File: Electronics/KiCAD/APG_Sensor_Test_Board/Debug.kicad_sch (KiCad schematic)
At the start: 0 parts

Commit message: debug schematic done
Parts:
- added BZ?: Buzzer, symbol Device:Buzzer
- added D? (x3): LED, symbol Device:LED
- added R? (x3): 200, symbol Device:R
- added R?: 10k, symbol Device:R
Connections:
- new net: BZ?.1 (+), R?.2
- new net: D?.2 (A), R?.2 (x3)
- new net Buzzer: R?.1
- new net Debug 1: R?.1
- new net Debug 2: R?.1
- new net Debug 3: R?.1
- new net GND: BZ?.2 (-), D?.1 (K), D?.1 (K), D?.1 (K)

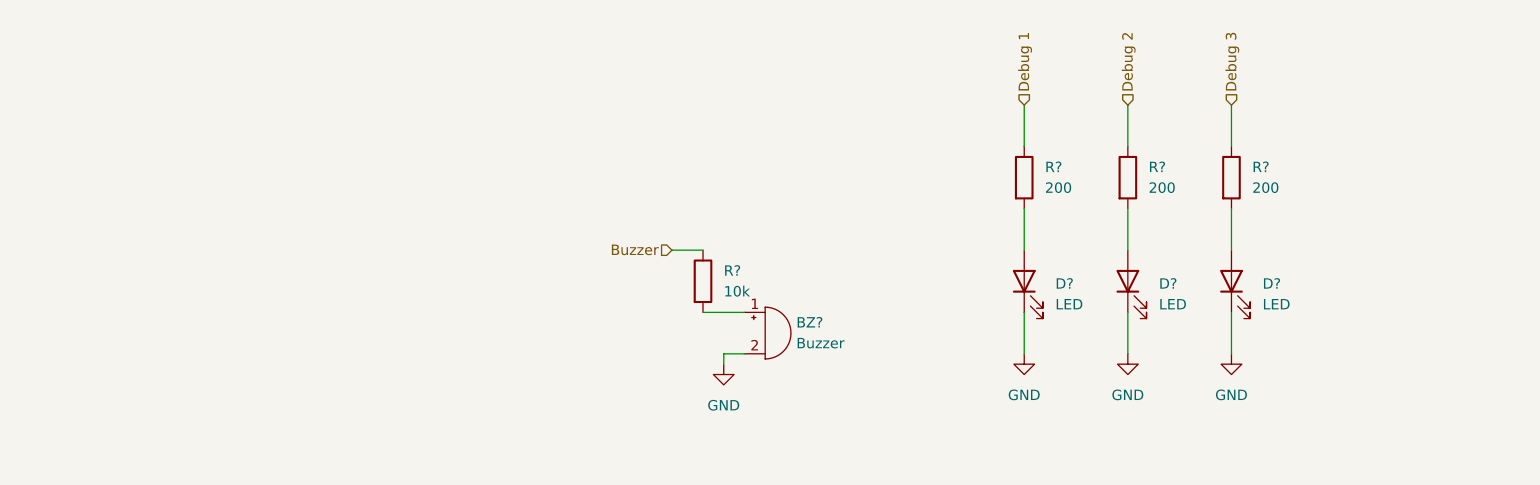
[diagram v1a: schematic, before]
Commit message: Gannon inspection decision to change IMU
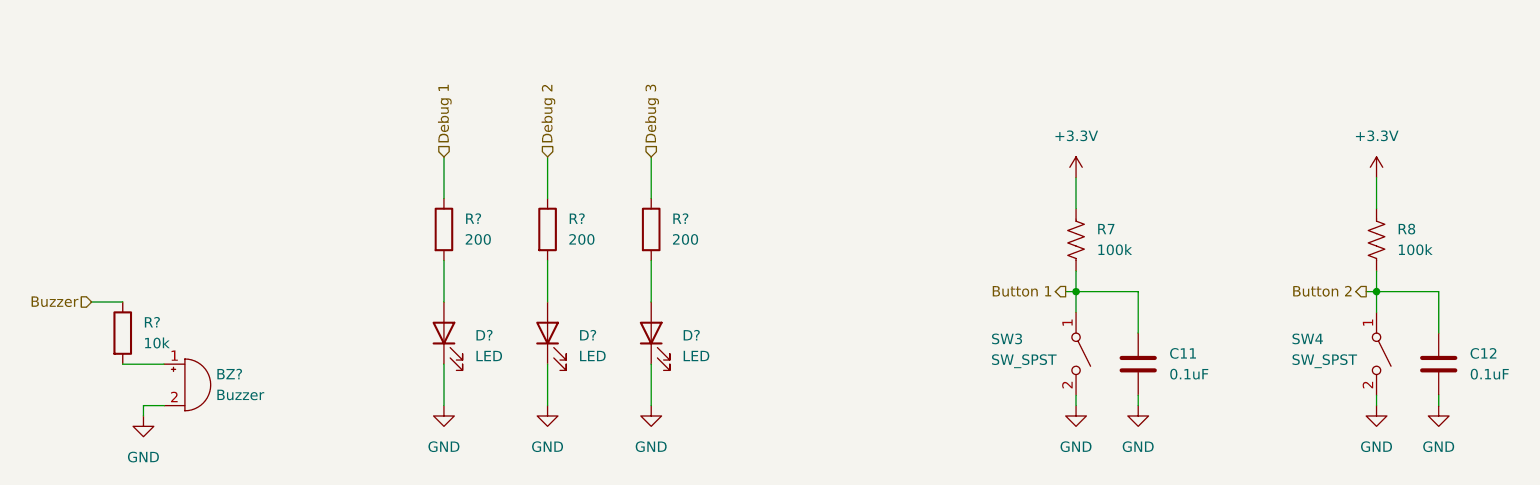
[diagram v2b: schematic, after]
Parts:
- added C11, C12: 0.1uF, symbol Device:C
- added R7, R8: 100k, symbol Device:R_US
- added SW3, SW4: SW_SPST, Button_Switch_SMD:SW_MEC_5GSH9, symbol Switch:SW_SPST
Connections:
- net GND: now also C11.2, C12.2, SW3.2 (B), SW4.2 (B)
- new net +3.3V: R7.1, R8.1
- new net Button 1: C11.1, R7.2, SW3.1 (A)
- new net Button 2: C12.1, R8.2, SW4.1 (A)
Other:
- moved on the sheet: BZ?, D?, R?

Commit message: reaninotate and begin footprints
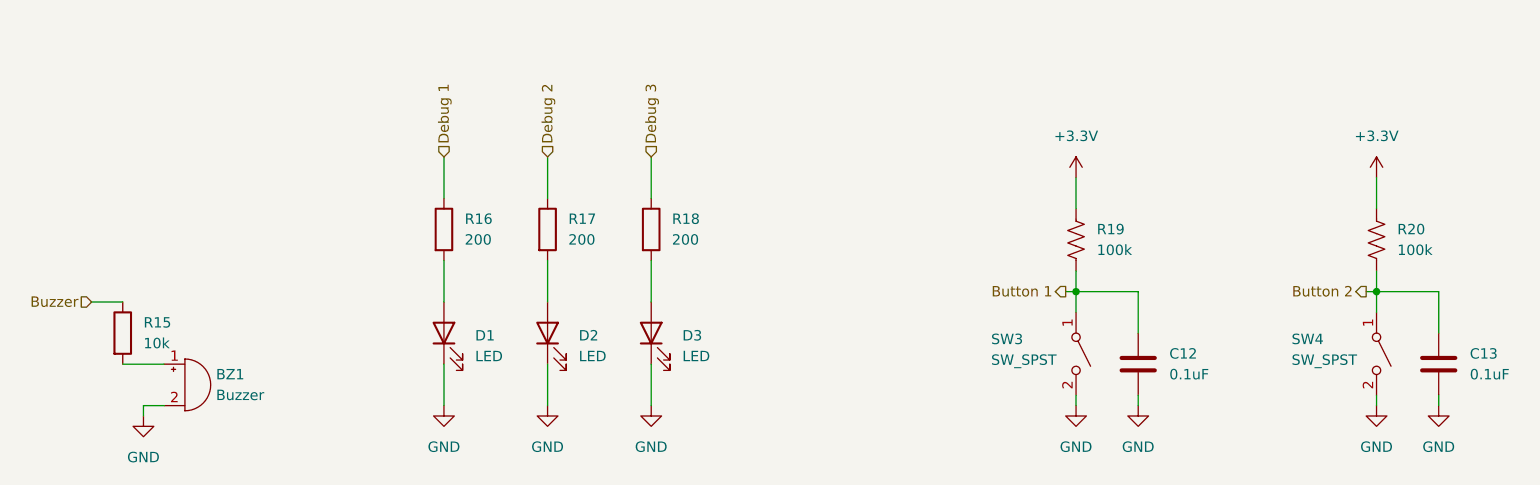
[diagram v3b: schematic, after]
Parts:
- C12: renamed from C11; footprint (none) -> Capacitor_SMD:C_0805_2012Metric
- C13: renamed from C12; footprint (none) -> Capacitor_SMD:C_0805_2012Metric
- R15, R16, R17, R18: renamed from R?; footprint (none) -> Resistor_SMD:R_0805_2012Metric
- R19: renamed from R7; footprint (none) -> Resistor_SMD:R_0805_2012Metric
- R20: renamed from R8; footprint (none) -> Resistor_SMD:R_0805_2012Metric
- gave numbers to parts that had none: 4
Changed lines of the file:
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@@
 		(dnp no)
 		(fields_autoplaced yes)
-		(property "Reference" "#PWR?"
+		(property "Reference" "#PWR036"
 			(at 106.68 101.6 0)
 			(effects
@@
 			(project "APG_Sensor_Test_Board"
 				(path "/3161be0c-372f-463d-be0a-bab00f344057/a925c584-3e41-45ac-af60-4ecbe46e87fc"
-					(reference "#PWR?")
+					(reference "#PWR036")
 					(unit 1)
 				)
@@
 		(dnp no)
 		(fields_autoplaced yes)
-		(property "Reference" "BZ?"
+		(property "Reference" "BZ1"
 			(at 78.74 91.4399 0)
 			(effects
@@
 			(project "APG_Sensor_Test_Board"
 				(path "/3161be0c-372f-463d-be0a-bab00f344057/a925c584-3e41-45ac-af60-4ecbe46e87fc"
-					(reference "BZ?")
+					(reference "BZ1")
 					(unit 1)
 				)
@@
 		(on_board yes)
 		(dnp no)
-		(property "Reference" "R7"
+		(property "Reference" "R19"
 			(at 186.69 73.6599 0)
 			(effects
@@
 			)
 		)
-		(property "Footprint" ""
+		(property "Footprint" "Resistor_SMD:R_0805_2012Metric"
 			(at 185.166 75.184 90)
 			(effects
@@
 			(project "APG_Sensor_Test_Board"
 				(path "/3161be0c-372f-463d-be0a-bab00f344057/a925c584-3e41-45ac-af60-4ecbe46e87fc"
-					(reference "R7")
+					(reference "R19")
 					(unit 1)
 				)
@@
 		(dnp no)
 		(fields_autoplaced yes)
-		(property "Reference" "#PWR031"
+		(property "Reference" "#PWR042"
 			(at 220.98 71.12 0)
 			(effects
@@
 			(project "APG_Sensor_Test_Board"
 				(path "/3161be0c-372f-463d-be0a-bab00f344057/a925c584-3e41-45ac-af60-4ecbe46e87fc"
-					(reference "#PWR031")
+					(reference "#PWR042")
 					(unit 1)
 				)
@@
 		(dnp no)
 		(fields_autoplaced yes)
-		(property "Reference" "#PWR032"
+		(property "Reference" "#PWR043"
 			(at 220.98 101.6 0)
 			(effects
@@
 			(project "APG_Sensor_Test_Board"
 				(path "/3161be0c-372f-463d-be0a-bab00f344057/a925c584-3e41-45ac-af60-4ecbe46e87fc"
-					(reference "#PWR032")
+					(reference "#PWR043")
 					(unit 1)
 				)
@@
 		(dnp no)
 		(fields_autoplaced yes)
-		(property "Reference" "#PWR029"
+		(property "Reference" "#PWR040"
 			(at 184.15 101.6 0)
 			(effects
@@
 			(project "APG_Sensor_Test_Board"
 				(path "/3161be0c-372f-463d-be0a-bab00f344057/a925c584-3e41-45ac-af60-4ecbe46e87fc"
-					(reference "#PWR029")
+					(reference "#PWR040")
 					(unit 1)
 				)
@@
 		(on_board yes)
 		(dnp no)
-		(property "Reference" "R8"
+		(property "Reference" "R20"
 			(at 223.52 73.6599 0)
 			(effects
@@
 			)
 		)
-		(property "Footprint" ""
+		(property "Footprint" "Resistor_SMD:R_0805_2012Metric"
 			(at 221.996 75.184 90)
 			(effects
@@
 			(project "APG_Sensor_Test_Board"
 				(path "/3161be0c-372f-463d-be0a-bab00f344057/a925c584-3e41-45ac-af60-4ecbe46e87fc"
-					(reference "R8")
+					(reference "R20")
 					(unit 1)
 				)
@@
 		(dnp no)
 		(fields_autoplaced yes)
-		(property "Reference" "R?"
+		(property "Reference" "R18"
 			(at 134.62 72.3899 0)
 			(effects
@@
 			)
 		)
-		(property "Footprint" ""
+		(property "Footprint" "Resistor_SMD:R_0805_2012Metric"
 			(at 130.302 73.66 90)
 			(effects
@@
 			(project "APG_Sensor_Test_Board"
 				(path "/3161be0c-372f-463d-be0a-bab00f344057/a925c584-3e41-45ac-af60-4ecbe46e87fc"
-					(reference "R?")
+					(reference "R18")
 					(unit 1)
 				)
@@
 		(dnp no)
 		(fields_autoplaced yes)
-		(property "Reference" "R?"
+		(property "Reference" "R15"
 			(at 69.85 85.0899 0)
 			(effects
@@
 			)
 		)
-		(property "Footprint" ""
+		(property "Footprint" "Resistor_SMD:R_0805_2012Metric"
 			(at 65.532 86.36 90)
 			(effects
@@
 			(project "APG_Sensor_Test_Board"
 				(path "/3161be0c-372f-463d-be0a-bab00f344057/a925c584-3e41-45ac-af60-4ecbe46e87fc"
-					(reference "R?")
+					(reference "R15")
 					(unit 1)
 				)
@@
 		(dnp no)
 		(fields_autoplaced yes)
-		(property "Reference" "#PWR?"
+		(property "Reference" "#PWR035"
 			(at 69.85 102.87 0)
 			(effects
@@
 			(project "APG_Sensor_Test_Board"
 				(path "/3161be0c-372f-463d-be0a-bab00f344057/a925c584-3e41-45ac-af60-4ecbe46e87fc"
-					(reference "#PWR?")
+					(reference "#PWR035")
 					(unit 1)
 				)
@@
 		(dnp no)
 		(fields_autoplaced yes)
-		(property "Reference" "#PWR?"
+		(property "Reference" "#PWR038"
 			(at 132.08 101.6 0)
 			(effects
@@
 			(project "APG_Sensor_Test_Board"
 				(path "/3161be0c-372f-463d-be0a-bab00f344057/a925c584-3e41-45ac-af60-4ecbe46e87fc"
-					(reference "#PWR?")
+					(reference "#PWR038")
 					(unit 1)
 				)
@@
 		(dnp no)
 		(fields_autoplaced yes)
-		(property "Reference" "#PWR?"
+		(property "Reference" "#PWR037"
 			(at 119.38 101.6 0)
 			(effects
@@
 			(project "APG_Sensor_Test_Board"
 				(path "/3161be0c-372f-463d-be0a-bab00f344057/a925c584-3e41-45ac-af60-4ecbe46e87fc"
-					(reference "#PWR?")
+					(reference "#PWR037")
 					(unit 1)
 				)
@@
 		(dnp no)
 		(fields_autoplaced yes)
-		(property "Reference" "R?"
+		(property "Reference" "R17"
 			(at 121.92 72.3899 0)
 			(effects
@@
 			)
 		)
-		(property "Footprint" ""
+		(property "Footprint" "Resistor_SMD:R_0805_2012Metric"
 			(at 117.602 73.66 90)
 			(effects
@@
 			(project "APG_Sensor_Test_Board"
 				(path "/3161be0c-372f-463d-be0a-bab00f344057/a925c584-3e41-45ac-af60-4ecbe46e87fc"
-					(reference "R?")
+					(reference "R17")
 					(unit 1)
 				)
@@
 		(dnp no)
 		(fields_autoplaced yes)
-		(property "Reference" "D?"
+		(property "Reference" "D2"
 			(at 123.19 86.6774 90)
 			(effects
@@
 			(project "APG_Sensor_Test_Board"
 				(path "/3161be0c-372f-463d-be0a-bab00f344057/a925c584-3e41-45ac-af60-4ecbe46e87fc"
-					(reference "D?")
+					(reference "D2")
 					(unit 1)
 				)
@@
 		(dnp no)
 		(fields_autoplaced yes)
-		(property "Reference" "D?"
+		(property "Reference" "D1"
 			(at 110.49 86.6774 90)
 			(effects
@@
 			(project "APG_Sensor_Test_Board"
 				(path "/3161be0c-372f-463d-be0a-bab00f344057/a925c584-3e41-45ac-af60-4ecbe46e87fc"
-					(reference "D?")
+					(reference "D1")
 					(unit 1)
 				)
@@
 		(dnp no)
 		(fields_autoplaced yes)
-		(property "Reference" "#PWR033"
+		(property "Reference" "#PWR044"
 			(at 228.6 101.6 0)
 			(effects
@@
 			(project "APG_Sensor_Test_Board"
 				(path "/3161be0c-372f-463d-be0a-bab00f344057/a925c584-3e41-45ac-af60-4ecbe46e87fc"
-					(reference "#PWR033")
+					(reference "#PWR044")
 					(unit 1)
 				)
@@
 		(dnp no)
 		(fields_autoplaced yes)
-		(property "Reference" "C12"
+		(property "Reference" "C13"
 			(at 232.41 88.8999 0)
 			(effects
@@
 			)
 		)
-		(property "Footprint" ""
+		(property "Footprint" "Capacitor_SMD:C_0805_2012Metric"
 			(at 229.5652 93.98 0)
 			(effects
@@
 			(project "APG_Sensor_Test_Board"
 				(path "/3161be0c-372f-463d-be0a-bab00f344057/a925c584-3e41-45ac-af60-4ecbe46e87fc"
-					(reference "C12")
+					(reference "C13")
 					(unit 1)
 				)
@@
 		(dnp no)
 		(fields_autoplaced yes)
-		(property "Reference" "C11"
+		(property "Reference" "C12"
 			(at 195.58 88.8999 0)
 			(effects
@@
 			)
 		)
-		(property "Footprint" ""
+		(property "Footprint" "Capacitor_SMD:C_0805_2012Metric"
 			(at 192.7352 93.98 0)
 			(effects
@@
 			(project "APG_Sensor_Test_Board"
 				(path "/3161be0c-372f-463d-be0a-bab00f344057/a925c584-3e41-45ac-af60-4ecbe46e87fc"
-					(reference "C11")
+					(reference "C12")
 					(unit 1)
 				)
@@
 		(dnp no)
 		(fields_autoplaced yes)
-		(property "Reference" "D?"
+		(property "Reference" "D3"
 			(at 135.89 86.6774 90)
 			(effects
@@
 			(project "APG_Sensor_Test_Board"
 				(path "/3161be0c-372f-463d-be0a-bab00f344057/a925c584-3e41-45ac-af60-4ecbe46e87fc"
-					(reference "D?")
+					(reference "D3")
 					(unit 1)
 				)
@@
 		(dnp no)
 		(fields_autoplaced yes)
-		(property "Reference" "R?"
+		(property "Reference" "R16"
 			(at 109.22 72.3899 0)
 			(effects
@@
 			)
 		)
-		(property "Footprint" ""
+		(property "Footprint" "Resistor_SMD:R_0805_2012Metric"
 			(at 104.902 73.66 90)
 			(effects
@@
 			(project "APG_Sensor_Test_Board"
 				(path "/3161be0c-372f-463d-be0a-bab00f344057/a925c584-3e41-45ac-af60-4ecbe46e87fc"
-					(reference "R?")
+					(reference "R16")
 					(unit 1)
 				)
@@
 		(dnp no)
 		(fields_autoplaced yes)
-		(property "Reference" "#PWR030"
+		(property "Reference" "#PWR041"
 			(at 191.77 101.6 0)
 			(effects
@@
 			(project "APG_Sensor_Test_Board"
 				(path "/3161be0c-372f-463d-be0a-bab00f344057/a925c584-3e41-45ac-af60-4ecbe46e87fc"
-					(reference "#PWR030")
+					(reference "#PWR041")
 					(unit 1)
 				)
@@
 		(dnp no)
 		(fields_autoplaced yes)
-		(property "Reference" "#PWR028"
+		(property "Reference" "#PWR039"
 			(at 184.15 71.12 0)
 			(effects
@@
 			(project "APG_Sensor_Test_Board"
 				(path "/3161be0c-372f-463d-be0a-bab00f344057/a925c584-3e41-45ac-af60-4ecbe46e87fc"
-					(reference "#PWR028")
-					(unit 1)
-				)
+					(reference "#PWR039")
+					(unit 1)
+				)

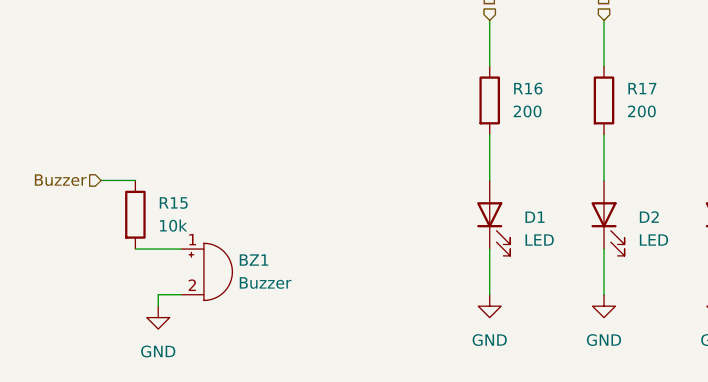
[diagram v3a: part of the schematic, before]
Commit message: completed footprint assignment
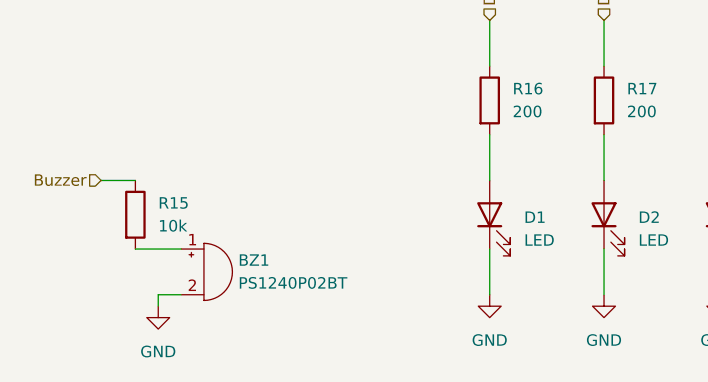
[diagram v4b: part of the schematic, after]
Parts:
- BZ1: value Buzzer -> PS1240P02BT; footprint (none) -> Buzzer_Beeper:Buzzer_TDK_PS1240P02BT_D12.2mm_H6.5mm
- D1, D2, D3: footprint (none) -> LED_SMD:LED_0805_2012Metric
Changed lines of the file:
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@@
 			)
 		)
-		(property "Value" "Buzzer"
+		(property "Value" "PS1240P02BT"
 			(at 78.74 93.9799 0)
 			(effects
@@
 			)
 		)
-		(property "Footprint" ""
+		(property "Footprint" "Buzzer_Beeper:Buzzer_TDK_PS1240P02BT_D12.2mm_H6.5mm"
 			(at 74.295 90.17 90)
 			(effects
@@
 		)
 		(property "Description" "Buzzer, polarized"
+			(at 74.93 92.71 0)
+			(effects
+				(font
+					(size 1.27 1.27)
+				)
+				(hide yes)
+			)
+		)
+		(property "JLCPCB" ""
 			(at 74.93 92.71 0)
 			(effects
@@
 			)
 		)
-		(property "Footprint" ""
+		(property "Footprint" "LED_SMD:LED_0805_2012Metric"
 			(at 119.38 86.36 0)
 			(effects
@@
 			)
 		)
-		(property "Footprint" ""
+		(property "Footprint" "LED_SMD:LED_0805_2012Metric"
 			(at 106.68 86.36 0)
 			(effects
@@
 			)
 		)
-		(property "Footprint" ""
+		(property "Footprint" "LED_SMD:LED_0805_2012Metric"
 			(at 132.08 86.36 0)
 			(effects

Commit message: JLC part numbers
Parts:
- D1: value LED -> Yellow; JLCPCB (none) -> C2296
- D2: value LED -> Green; JLCPCB (none) -> C2297
- D3: value LED -> Red; JLCPCB (none) -> C84256
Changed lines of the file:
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@@
 			)
 		)
-		(property "Value" "LED"
+		(property "Value" "Green"
 			(at 123.19 89.2174 90)
 			(effects
@@
 		)
 		(property "Description" "Light emitting diode"
+			(at 119.38 86.36 0)
+			(effects
+				(font
+					(size 1.27 1.27)
+				)
+				(hide yes)
+			)
+		)
+		(property "JLCPCB" "C2297"
 			(at 119.38 86.36 0)
 			(effects
@@
 			)
 		)
-		(property "Value" "LED"
+		(property "Value" "Yellow"
 			(at 110.49 89.2174 90)
 			(effects
@@
 		)
 		(property "Description" "Light emitting diode"
+			(at 106.68 86.36 0)
+			(effects
+				(font
+					(size 1.27 1.27)
+				)
+				(hide yes)
+			)
+		)
+		(property "JLCPCB" "C2296"
 			(at 106.68 86.36 0)
 			(effects
@@
 			)
 		)
-		(property "Value" "LED"
+		(property "Value" "Red"
 			(at 135.89 89.2174 90)
 			(effects
@@
 			(at 132.08 86.36 0)
 			(effects
+				(font
+					(size 1.27 1.27)
+				)
+				(hide yes)
+			)
+		)
+		(property "JLCPCB" "C84256"
+			(at 132.08 86.36 0)
+			(effects

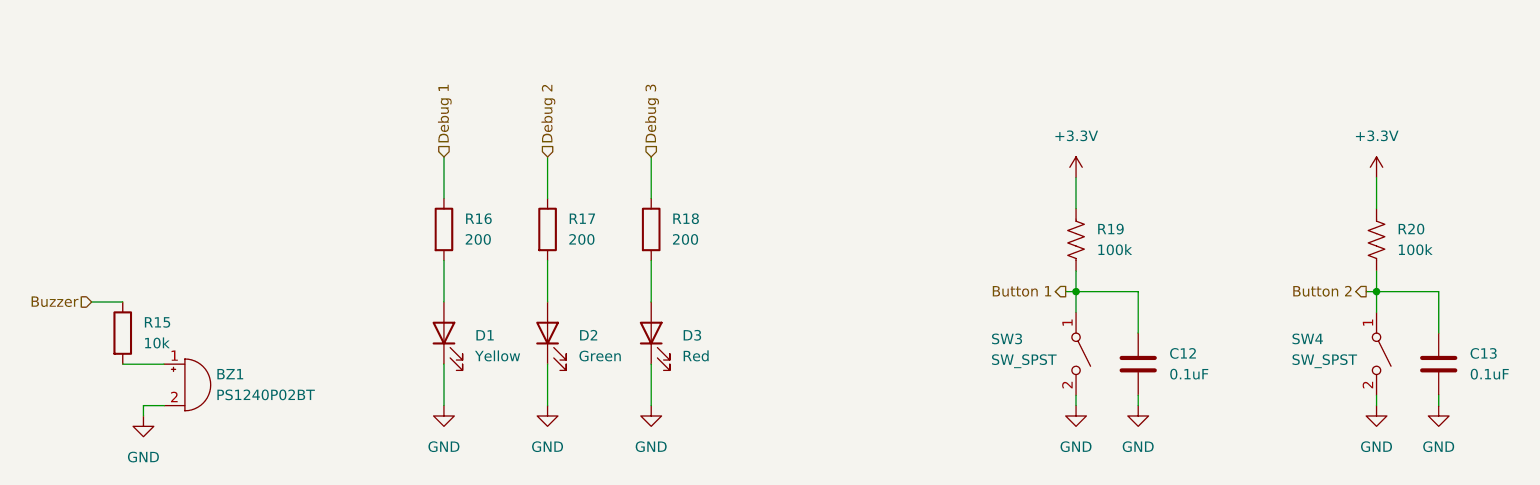
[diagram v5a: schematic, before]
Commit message: MOved IMU and HIGH G to SPI other misc changes
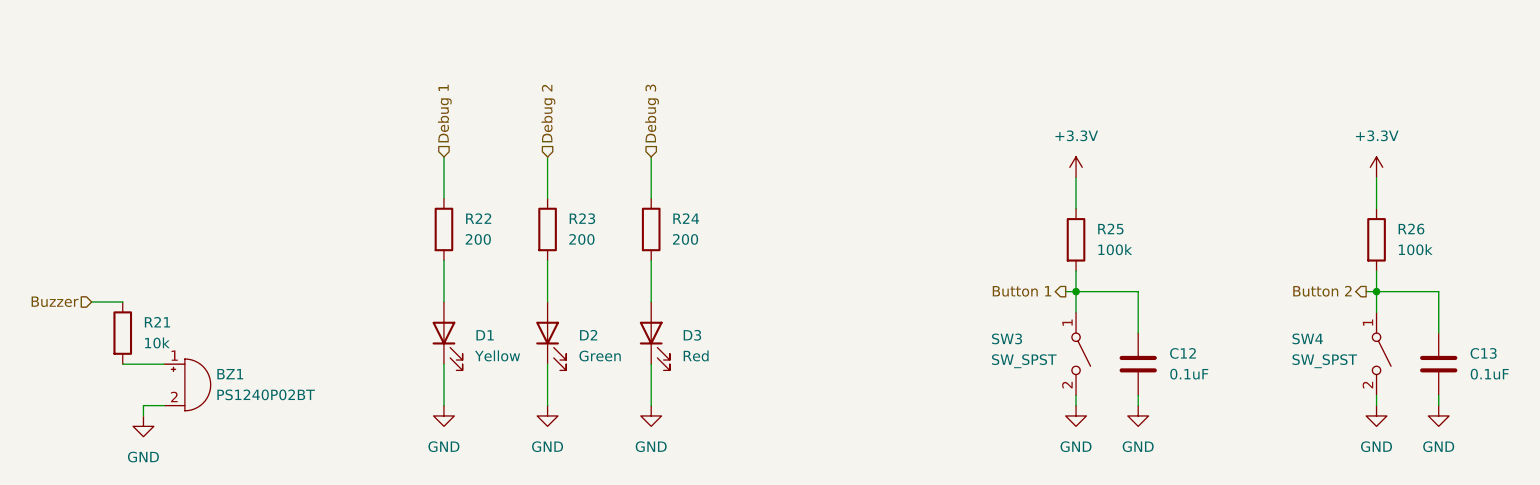
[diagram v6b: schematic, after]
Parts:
- removed R19, R20: 100k, Resistor_SMD:R_0805_2012Metric, symbol Device:R_US
- added R25, R26: 100k, Resistor_SMD:R_0805_2012Metric, symbol Device:R
- renumbered R15 to R21, R16 to R22, R17 to R23, R18 to R24
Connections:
- net +3.3V: now also R25.1, R26.1
- net Button 1: now also R25.2
- net Button 2: now also R26.2

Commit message: TVS protection began layout
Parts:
- SW3, SW4: footprint Button_Switch_SMD:SW_MEC_5GSH9 -> Button_Switch_THT:SW_PUSH_6mm_H5mm
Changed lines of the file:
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@@
 			)
 		)
-		(property "Footprint" "Button_Switch_SMD:SW_MEC_5GSH9"
+		(property "Footprint" "Button_Switch_THT:SW_PUSH_6mm_H5mm"
 			(at 184.15 88.9 0)
 			(effects
@@
 			)
 		)
-		(property "Footprint" "Button_Switch_SMD:SW_MEC_5GSH9"
+		(property "Footprint" "Button_Switch_THT:SW_PUSH_6mm_H5mm"
 			(at 220.98 88.9 0)
 			(effects
